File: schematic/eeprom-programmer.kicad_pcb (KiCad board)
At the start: 2 copper layers, 8 parts, among them IC1 AT28C64B-15PU, U1 74HC595, U2 74HC595

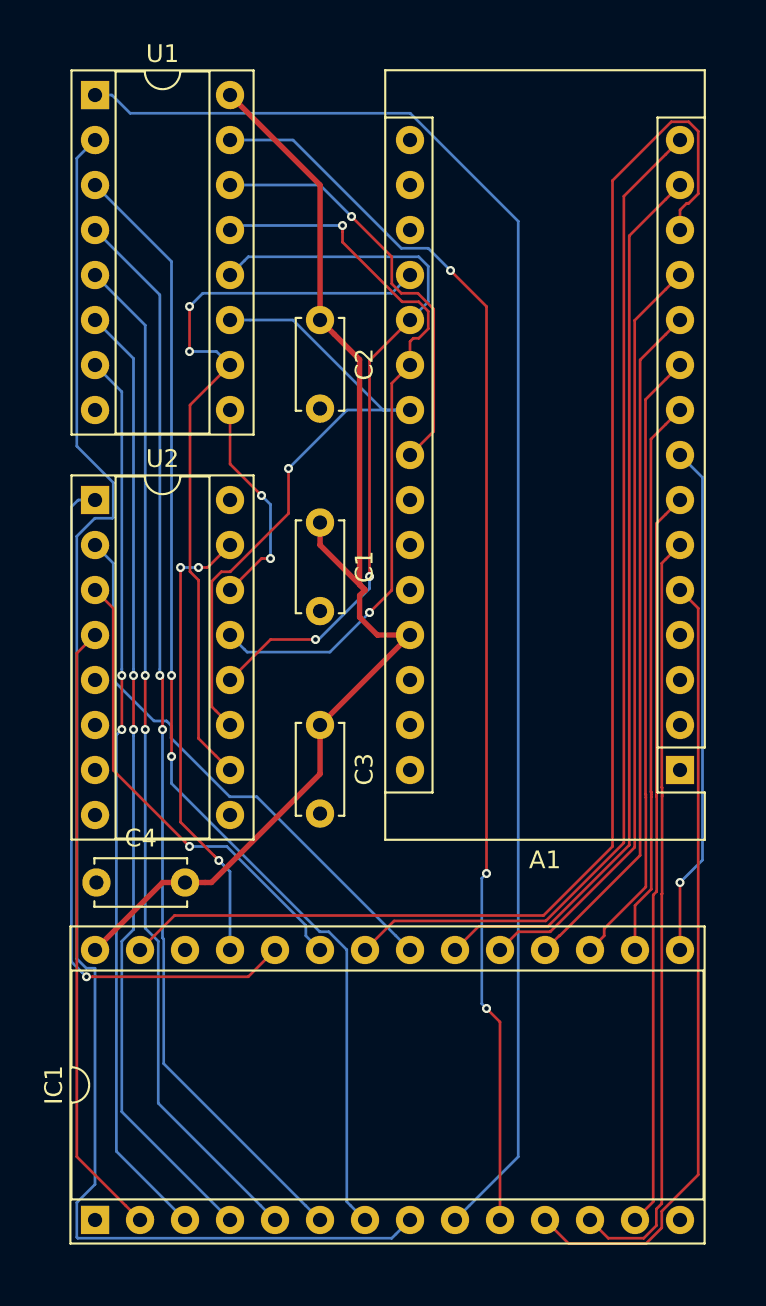
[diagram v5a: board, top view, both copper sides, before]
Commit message: Add edge cuts
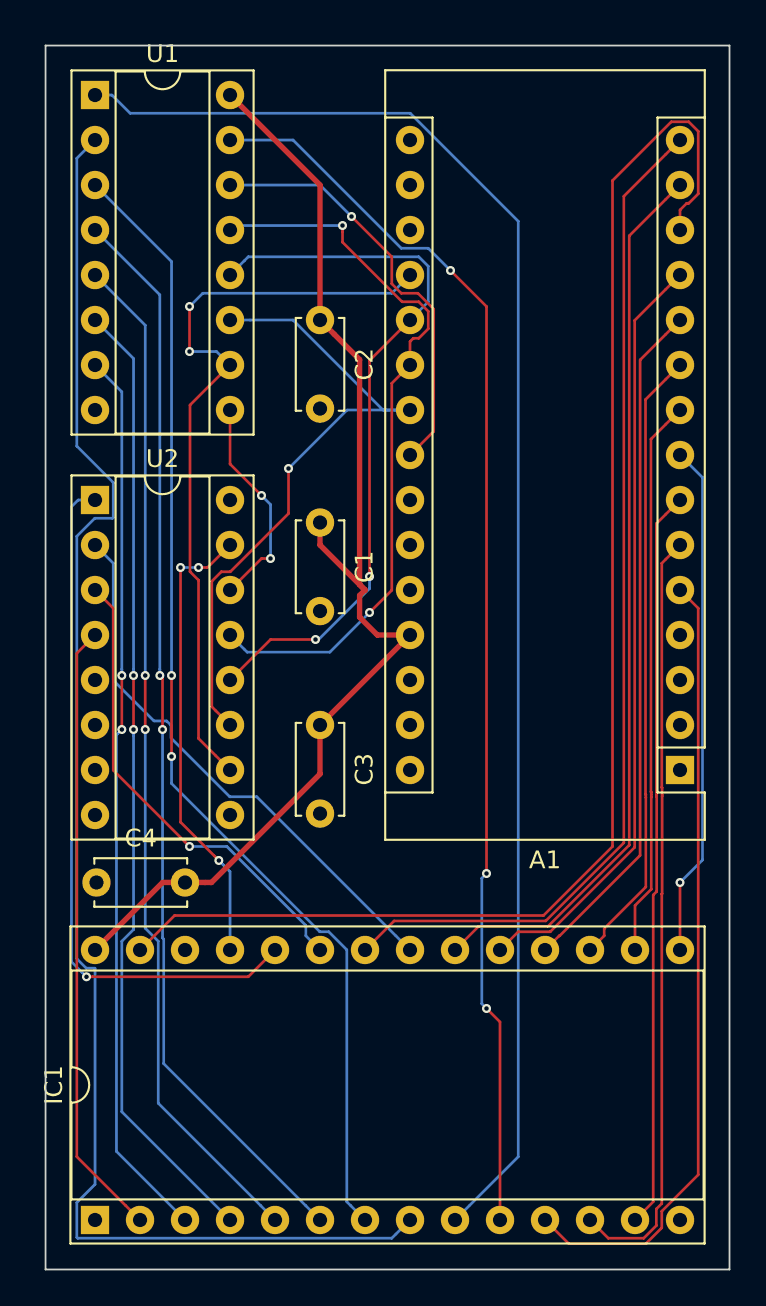
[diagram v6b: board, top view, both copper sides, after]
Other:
- board outline added: 38.6 x 69.1 mm
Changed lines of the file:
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@@
   (general
     (thickness 1.6)
-    (drawings 0)
+    (drawings 4)
     (tracks 331)
     (zones 0)
@@
     )
   )
+  (gr_line (start 92.456 136.144) (end 92.456 67.056) (layer Edge.Cuts) (width 0.1))
+  (gr_line (start 131.064 136.144) (end 92.456 136.144) (layer Edge.Cuts) (width 0.1))
+  (gr_line (start 131.064 67.056) (end 131.064 136.144) (layer Edge.Cuts) (width 0.1))
+  (gr_line (start 92.456 67.056) (end 131.064 67.056) (layer Edge.Cuts) (width 0.1))
   (via (at 100.584 81.788) (size 0.508) (drill 0.254) (layers F.Cu B.Cu) (net 1))
   (segment (start 101.332899 81.039101) (end 100.584 81.788) (width 0.1534) (layer B.Cu) (net 1))

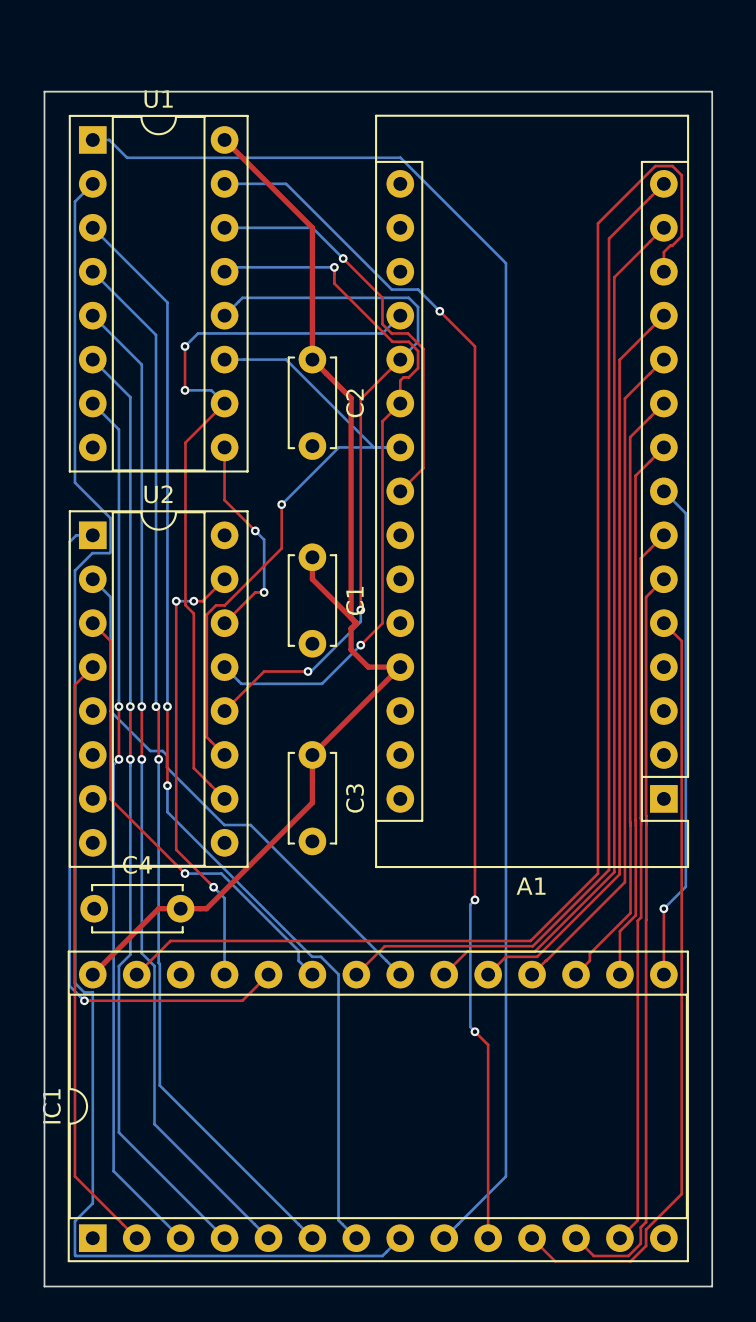
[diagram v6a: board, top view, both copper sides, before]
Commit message: Add ground fills and silkscreen
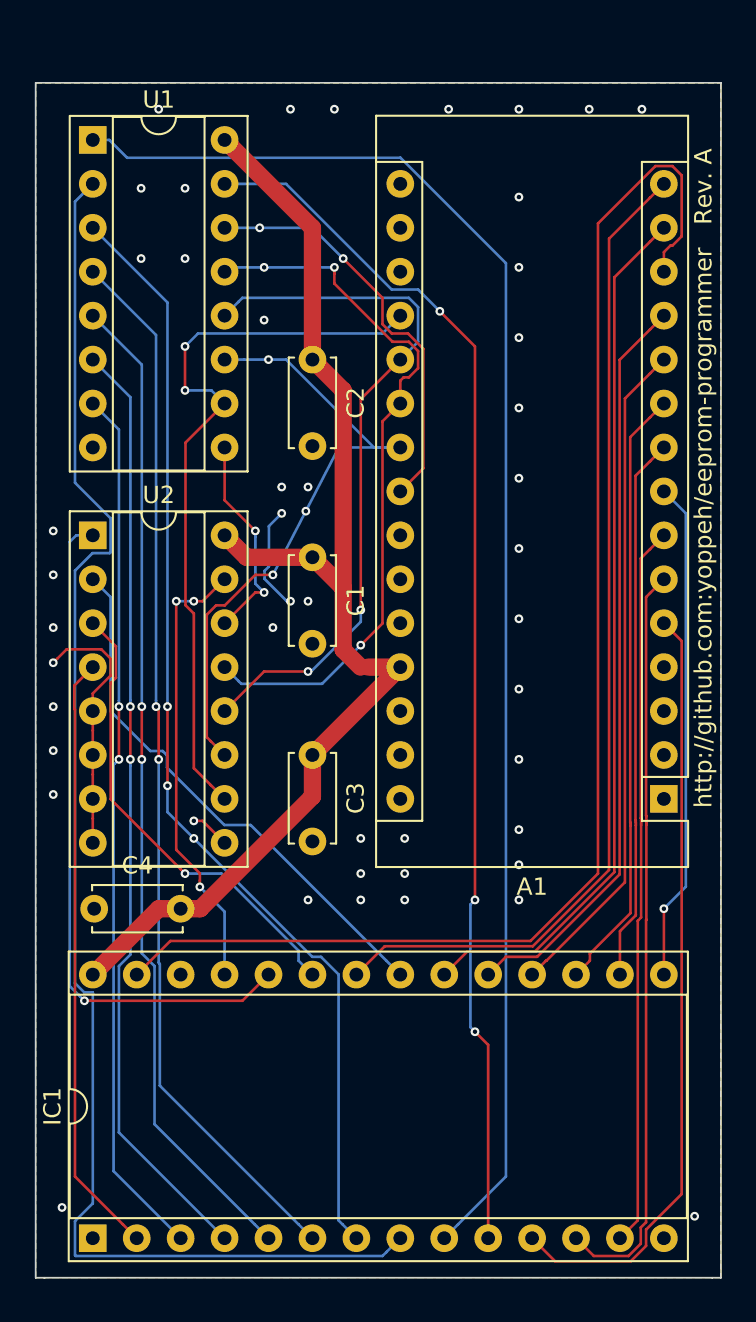
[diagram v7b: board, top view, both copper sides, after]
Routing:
- net GND: track 0.00 -> 23.5 mm, vias 0 -> 47
- net Arduino5V: track 67.6 -> 70.3 mm
- net srSerialClock: track 37.5 -> 37.4 mm, vias 1 -> 3
- net srSerialData: vias 1 -> 2
- net srNotOutputEnable: vias 2 -> 3
- net /addr03: vias 2 -> 3
- added copper zone on B.Cu, net GND
- added copper zone on F.Cu, net GND
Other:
- board size 38.6 x 69.1 mm -> 39.6 x 69.1 mm
- board text added: "http://github.com:yoppeh/eeprom-programmer Rev. A"

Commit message: Update solder mask clearance for Osh Park specs
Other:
- rule pad_to_mask_clearance: 0 -> 0.0508
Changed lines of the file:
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@@
     (pad_size 1.6 1.6)
     (pad_drill 0.8)
-    (pad_to_mask_clearance 0)
+    (pad_to_mask_clearance 0.0508)
     (aux_axis_origin 0 0)
     (visible_elements 7FFFFFFF)
